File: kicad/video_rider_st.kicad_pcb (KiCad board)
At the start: 2 copper layers, 99 x 92.1 mm, 43 parts, among them J1 F3311A7H121020E200, J2 F3311A7H121020E200, J3 Conn_01x02_Male, J4 Conn_01x03_Male, J5 F3311A7H121020E200, J6 F3311A7H121020E200, J7 Conn_01x06_Male, U1 ST_SHIFTER_PHY, U10 ST_GLUE_SOCKET, U2 ST_SHIFTER_SOCKET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

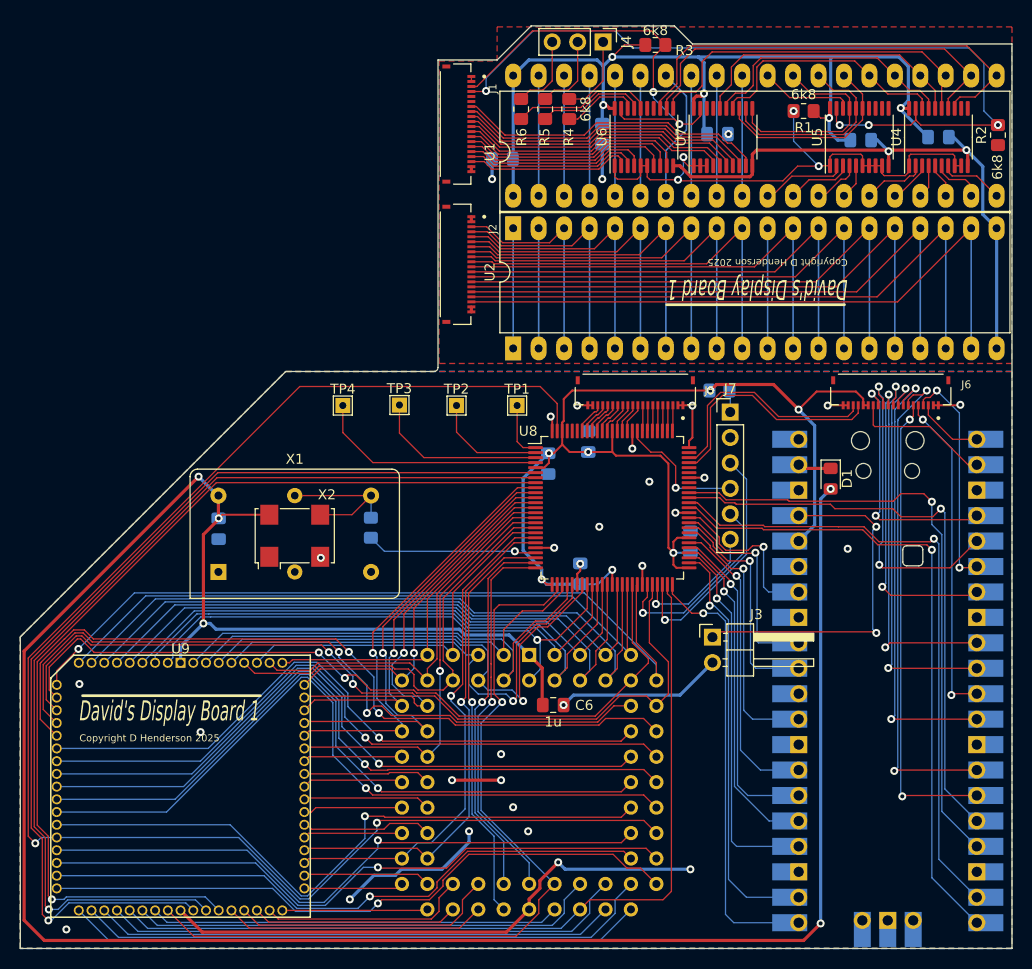
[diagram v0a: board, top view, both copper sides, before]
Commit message: Passing DRC with corrected PLCC orientation.
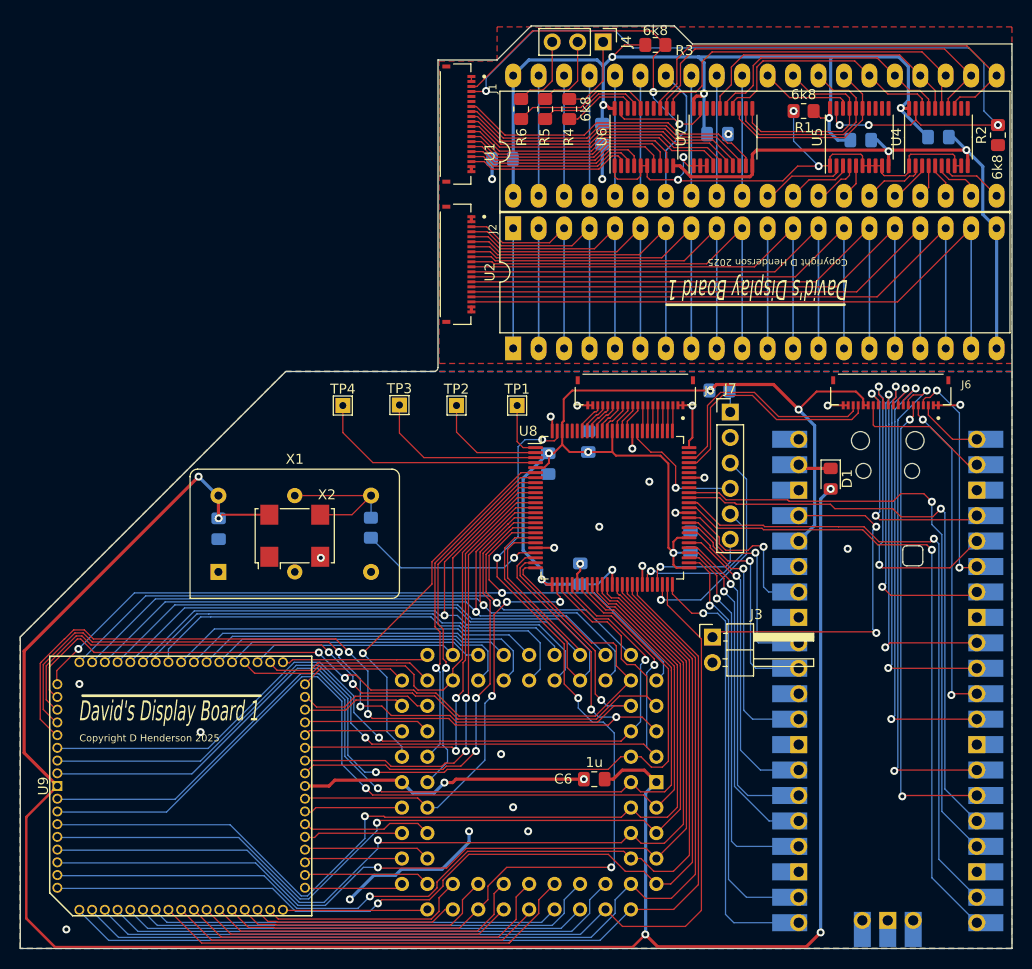
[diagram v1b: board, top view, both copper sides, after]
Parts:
- moved U10 18.0 mm to (163.1, 127.6), turned to 90 degrees
- moved U9 17.4 mm to (103.3, 128.0), turned to 90 degrees
- moved C6 8.46 mm to (156.9, 127.3), turned to 180 degrees
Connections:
- U8 pad 10: /A2 -> /LDS
- U8 pad 11: /A3 -> /UDS
- U8 pad 12: /A4 -> /VSYNC_OUT
- U8 pad 13: /A5 -> /HSYNC_OUT
- U8 pad 14: /A6 -> /A3
- U8 pad 15: /A7 -> /A4
- U8 pad 16: /RW_C -> /BLANK_OUT
- U8 pad 17: /A9 -> /A5
- U8 pad 18: /A8 -> /A6
- U8 pad 19: /LDS -> /A2
- U8 pad 20: /UDS -> /A1
- U8 pad 23: /HSYNC -> /A10
- U8 pad 24: /VSYNC -> /A9
- U8 pad 25: /BLANK -> /A7
- U8 pad 28: /A12 -> /A8
- U8 pad 29: /A13 -> /A11
- U8 pad 30: /A10 -> /A12
- U8 pad 32: /A11 -> /A13
- U8 pad 46: /AS -> unconnected-(U8-Pad46)
- U8 pad 49: /DTACK -> /AS
- U8 pad 6: /BLANK_OUT -> /HSYNC
- U8 pad 7: /HSYNC_OUT -> /VSYNC
- U8 pad 8: /VSYNC_OUT -> /BLANK
- U8 pad 9: /A1 -> /RW_C
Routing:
- net /DTACK: track 87.2 -> 9.89 mm
- net /RESET: track 155.3 -> 95.5 mm, vias 2 -> 4
- net /BLANK_OUT: track 100.3 -> 45.5 mm, vias 1 -> 2
- net /VSYNC_OUT: track 98.8 -> 44.3 mm, vias 1 -> 2
- net /HSYNC_OUT: track 99.6 -> 45.3 mm, vias 1 -> 2
- net /A8: track 37.6 -> 89.6 mm, vias 0 -> 2
- net /A10: track 49.1 -> 100.6 mm, vias 1 -> 4
- net /FCS: track 64.8 -> 14.4 mm, vias 1 -> 0
- net /A9: track 44.4 -> 94.2 mm, vias 0 -> 3
- net /A12: track 42.2 -> 91.3 mm, vias 0 -> 2
- net /GND_C: track 117.1 -> 68.5 mm, vias 28 -> 25
- net /BGI: track 57.6 -> 9.30 mm
- net /A15: track 53.1 -> 101.4 mm, vias 0 -> 1
- net /A7: track 39.1 -> 85.6 mm, vias 0 -> 2
- net /A13: track 50.0 -> 96.1 mm, vias 0 -> 1
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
